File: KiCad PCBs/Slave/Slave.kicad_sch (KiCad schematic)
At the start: 47 parts, among them J1 Screw_Terminal_01x02, J10 AVR-ISP-6, J11 Conn_01x06_Female, J12 Screw_Terminal_01x02, J13 Screw_Terminal_01x02, J14 Screw_Terminal_01x02, J15 Screw_Terminal_01x02, J16 Screw_Terminal_01x02, J2 Screw_Terminal_01x02, J3 Screw_Terminal_01x02, J4 Screw_Terminal_01x02, J5 Screw_Terminal_01x02, J6 Screw_Terminal_01x02, J7 Screw_Terminal_01x02, J8 Screw_Terminal_01x02, J9 Screw_Terminal_01x02, SW1 SW_DIP_x02, SW2 SW_DIP_x02, SW3 SW_MEC_5E, U1 ATmega328P-AU, U2 MAX487ESA+T, U3 ULN2003A, U5 AMS1117-5.0, Y1 Crystal_GND24

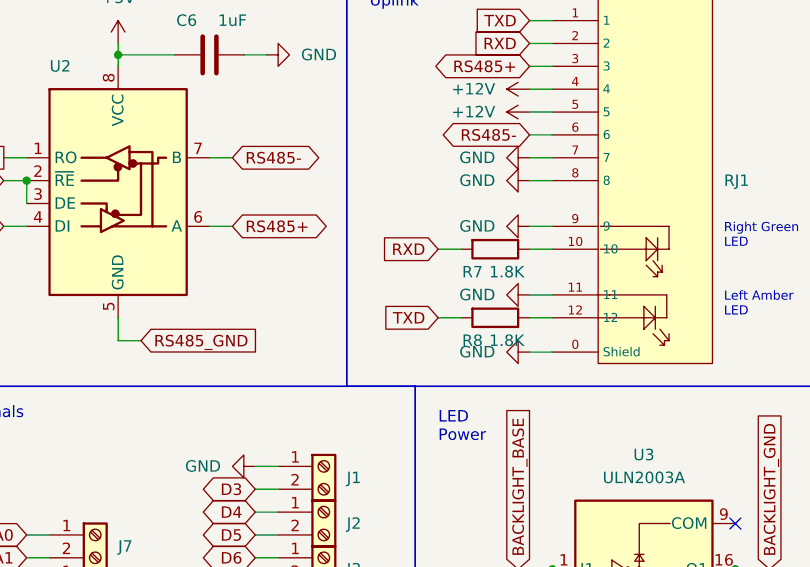
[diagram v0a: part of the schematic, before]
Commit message: Fixed swapped LEDs on Slave
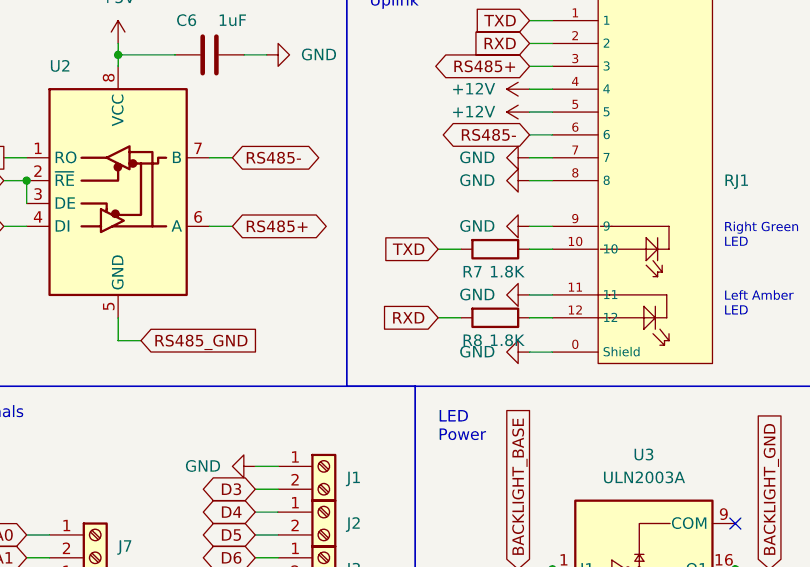
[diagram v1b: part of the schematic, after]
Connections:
- net RXD: now also R8.2; no longer R7.2
- net TXD: now also R7.2; no longer R8.2
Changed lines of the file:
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@@
+    )
+  )
+  (global_label "TXD" (shape input) (at 242.57 43.18 180) (fields_autoplaced)
+    (effects (font (size 1.27 1.27)) (justify right))
+    (property "Intersheet References" "${INTERSHEET_REFS}" (id 0) (at 236.7098 43.1006 0)
+      (effects (font (size 1.27 1.27)) (justify right) hide)
     )
   )
@@
     )
   )
-  (global_label "TXD" (shape input) (at 242.57 50.8 180) (fields_autoplaced)
-    (effects (font (size 1.27 1.27)) (justify right))
-    (property "Intersheet References" "${INTERSHEET_REFS}" (id 0) (at 236.7098 50.7206 0)
-      (effects (font (size 1.27 1.27)) (justify right) hide)
-    )
-  )
   (global_label "D10" (shape bidirectional) (at 222.25 87.63 180) (fields_autoplaced)
     (effects (font (size 1.27 1.27)) (justify right))
@@
     )
   )
-  (global_label "RXD" (shape input) (at 242.57 43.18 180) (fields_autoplaced)
-    (effects (font (size 1.27 1.27)) (justify right))
-    (property "Intersheet References" "${INTERSHEET_REFS}" (id 0) (at 236.4074 43.1006 0)
-      (effects (font (size 1.27 1.27)) (justify right) hide)
-    )
-  )
   (global_label "A3" (shape bidirectional) (at 196.85 82.55 180) (fields_autoplaced)
     (effects (font (size 1.27 1.27)) (justify right))
@@
       (effects (font (size 1.27 1.27)) (justify right) hide)
     )
+  )
+  (global_label "RXD" (shape input) (at 242.57 50.8 180) (fields_autoplaced)
+    (effects (font (size 1.27 1.27)) (justify right))
+    (property "Intersheet References" "${INTERSHEET_REFS}" (id 0) (at 236.4074 50.7206 0)
+      (effects (font (size 1.27 1.27)) (justify right) hide)
+    )

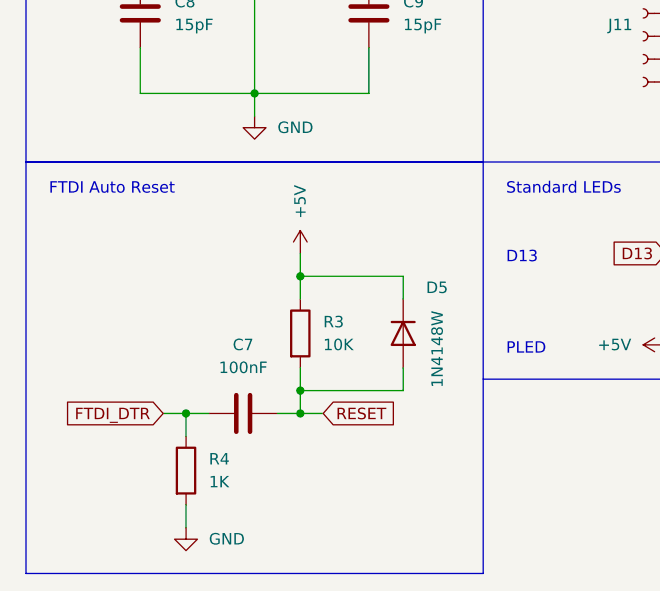
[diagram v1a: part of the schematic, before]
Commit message: Removed unnecessary resistor
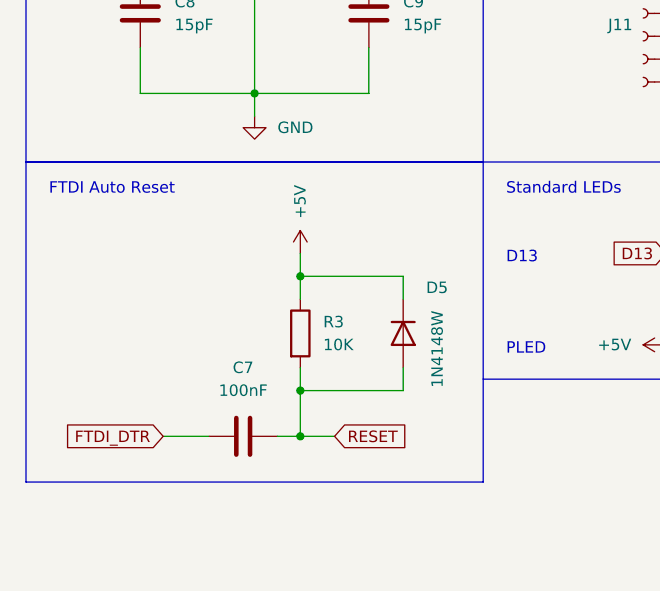
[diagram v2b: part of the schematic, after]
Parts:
- removed R4: 1K, Resistor_SMD:R_0805_2012Metric, symbol Device:R
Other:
- moved on the sheet: C7
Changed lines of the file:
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@@
   (junction (at 38.1 78.74) (diameter 0) (color 0 0 0 0)
   )
-  (junction (at 43.18 154.94) (diameter 0) (color 0 0 0 0)
+  (junction (at 43.18 157.48) (diameter 0) (color 0 0 0 0)
   )
   (junction (at 87.63 35.56) (diameter 0) (color 0 0 0 0)
@@
   (junction (at 27.94 35.56) (diameter 0) (color 0 0 0 0)
   )
-  (junction (at 30.48 154.94) (diameter 0) (color 0 0 0 0)
-  )
   (no_connect (at 48.26 22.86))
   (no_connect (at 133.35 69.85))
@@
     (stroke (width 0) (type default) (color 0 0 0 0))
   )
-  (wire (pts (xy 43.18 154.94) (xy 43.18 152.4))
+  (wire (pts (xy 43.18 157.48) (xy 43.18 152.4))
     (stroke (width 0) (type default) (color 0 0 0 0))
   )
@@
     (stroke (width 0) (type default) (color 0 0 0 0))
   )
-  (wire (pts (xy 30.48 154.94) (xy 33.02 154.94))
-    (stroke (width 0) (type default) (color 0 0 0 0))
-  )
   (polyline (pts (xy 185.42 12.7) (xy 185.42 41.91))
     (stroke (width 0) (type default) (color 0 0 0 0))
@@
     (stroke (width 0) (type default) (color 0 0 0 0))
   )
-  (wire (pts (xy 27.94 154.94) (xy 30.48 154.94))
+  (wire (pts (xy 27.94 157.48) (xy 33.02 157.48))
     (stroke (width 0) (type default) (color 0 0 0 0))
   )
@@
     (stroke (width 0) (type default) (color 0 0 0 0))
   )
-  (polyline (pts (xy 12.7 127) (xy 12.7 172.72))
+  (polyline (pts (xy 12.7 127) (xy 12.7 162.56))
     (stroke (width 0) (type default) (color 0 0 0 0))
   )
@@
     (stroke (width 0) (type default) (color 0 0 0 0))
   )
-  (polyline (pts (xy 63.5 172.72) (xy 12.7 172.72))
+  (polyline (pts (xy 63.5 162.56) (xy 12.7 162.56))
     (stroke (width 0) (type default) (color 0 0 0 0))
   )
@@
     (stroke (width 0) (type default) (color 0 0 0 0))
   )
-  (wire (pts (xy 30.48 167.64) (xy 30.48 165.1))
-    (stroke (width 0) (type default) (color 0 0 0 0))
-  )
   (wire (pts (xy 50.8 101.6) (xy 53.34 101.6))
     (stroke (width 0) (type default) (color 0 0 0 0))
@@
     (stroke (width 0) (type default) (color 0 0 0 0))
   )
-  (wire (pts (xy 30.48 154.94) (xy 30.48 157.48))
-    (stroke (width 0) (type default) (color 0 0 0 0))
-  )
   (wire (pts (xy 224.79 111.76) (xy 224.79 114.3))
     (stroke (width 0) (type default) (color 0 0 0 0))
@@
     (stroke (width 0) (type default) (color 0 0 0 0))
   )
-  (polyline (pts (xy 63.5 127) (xy 63.5 172.72))
+  (polyline (pts (xy 63.5 127) (xy 63.5 162.56))
     (stroke (width 0) (type default) (color 0 0 0 0))
   )
@@
     (stroke (width 0) (type default) (color 0 0 0 0))
   )
-  (wire (pts (xy 43.18 154.94) (xy 45.72 154.94))
+  (wire (pts (xy 43.18 157.48) (xy 46.99 157.48))
     (stroke (width 0) (type default) (color 0 0 0 0))
   )
@@
     (stroke (width 0) (type default) (color 0 0 0 0))
   )
-  (wire (pts (xy 40.64 154.94) (xy 43.18 154.94))
+  (wire (pts (xy 40.64 157.48) (xy 43.18 157.48))
     (stroke (width 0) (type default) (color 0 0 0 0))
   )
@@
     )
   )
-  (global_label "FTDI_DTR" (shape input) (at 27.94 154.94 180) (fields_autoplaced)
+  (global_label "FTDI_DTR" (shape input) (at 27.94 157.48 180) (fields_autoplaced)
     (effects (font (size 1.27 1.27)) (justify right))
-    (property "Intersheet References" "${INTERSHEET_REFS}" (id 0) (at 17.1207 154.8606 0)
+    (property "Intersheet References" "${INTERSHEET_REFS}" (id 0) (at 17.1207 157.4006 0)
       (effects (font (size 1.27 1.27)) (justify right) hide)
     )
@@
     )
   )
-  (global_label "RESET" (shape input) (at 45.72 154.94 0) (fields_autoplaced)
+  (global_label "RESET" (shape input) (at 46.99 157.48 0) (fields_autoplaced)
     (effects (font (size 1.27 1.27)) (justify left))
-    (property "Intersheet References" "${INTERSHEET_REFS}" (id 0) (at 53.8783 154.8606 0)
+    (property "Intersheet References" "${INTERSHEET_REFS}" (id 0) (at 55.1483 157.4006 0)
       (effects (font (size 1.27 1.27)) (justify left) hide)
     )
@@
     (pin "4")
   )
-  (symbol (lib_id "Device:C") (at 36.83 154.94 270) (unit 1)
+  (symbol (lib_id "Device:C") (at 36.83 157.48 270) (unit 1)
     (in_bom yes) (on_board yes) (fields_autoplaced)
-    (property "Reference" "C7" (id 0) (at 36.83 147.32 90))
-    (property "Value" "100nF" (id 1) (at 36.83 149.86 90))
-    (property "Footprint" "A10 KiCad Libraries:C0402" (id 2) (at 33.02 155.9052 0)
+    (property "Reference" "C7" (id 0) (at 36.83 149.86 90))
+    (property "Value" "100nF" (id 1) (at 36.83 152.4 90))
+    (property "Footprint" "A10 KiCad Libraries:C0402" (id 2) (at 33.02 158.4452 0)
       (effects (font (size 1.27 1.27)) hide)
     )
-    (property "Datasheet" "~" (id 3) (at 36.83 154.94 0)
+    (property "Datasheet" "~" (id 3) (at 36.83 157.48 0)
       (effects (font (size 1.27 1.27)) hide)
     )
-    (property "LCSC" "C1525" (id 4) (at 36.83 154.94 0)
+    (property "LCSC" "C1525" (id 4) (at 36.83 157.48 0)
       (effects (font (size 1.27 1.27)) hide)
     )
@@
     (pin "2")
   )
-  (symbol (lib_id "Device:R") (at 30.48 161.29 0) (unit 1)
-    (in_bom yes) (on_board yes) (fields_autoplaced)
-    (property "Reference" "R4" (id 0) (at 33.02 160.0199 0)
-      (effects (font (size 1.27 1.27)) (justify left))
-    )
-    (property "Value" "1K" (id 1) (at 33.02 162.5599 0)
-      (effects (font (size 1.27 1.27)) (justify left))
-    )
-    (property "Footprint" "Resistor_SMD:R_0805_2012Metric" (id 2) (at 28.702 161.29 90)
-      (effects (font (size 1.27 1.27)) hide)
-    )
-    (property "Datasheet" "~" (id 3) (at 30.48 161.29 0)
-      (effects (font (size 1.27 1.27)) hide)
-    )
-    (property "LCSC" "C17513" (id 4) (at 30.48 161.29 0)
-      (effects (font (size 1.27 1.27)) hide)
-    )
-    (pin "1")
-    (pin "2")
-  )
   (symbol (lib_id "Connector:Screw_Terminal_01x02") (at 201.93 119.38 270) (unit 1)
     (in_bom yes) (on_board yes)
@@
     (pin "3")
   )
-  (symbol (lib_id "power:GND") (at 30.48 167.64 0) (unit 1)
-    (in_bom yes) (on_board yes) (fields_autoplaced)
-    (property "Reference" "#PWR0102" (id 0) (at 30.48 173.99 0)
-      (effects (font (size 1.27 1.27)) hide)
-    )
-    (property "Value" "GND" (id 1) (at 33.02 168.9099 0)
-      (effects (font (size 1.27 1.27)) (justify left))
-    )
-    (property "Footprint" "" (id 2) (at 30.48 167.64 0)
-      (effects (font (size 1.27 1.27)) hide)
-    )
-    (property "Datasheet" "" (id 3) (at 30.48 167.64 0)
-      (effects (font (size 1.27 1.27)) hide)
-    )
-    (pin "1")
-  )
   (symbol (lib_id "Device:C_Polarized") (at 68.58 31.75 0) (unit 1)
     (in_bom yes) (on_board yes)
@@
       (reference "#PWR0101") (unit 1) (value "+5V") (footprint "")
     )
-    (path "/df391fcf-55bf-4a0a-9ae3-03317be1cd1b"
-      (reference "#PWR0102") (unit 1) (value "GND") (footprint "")
-    )
     (path "/1d7d13da-6155-4f5e-b055-b0667fd2dc2b"
       (reference "#PWR0103") (unit 1) (value "+12V") (footprint "")
@@
       (reference "R3") (unit 1) (value "10K") (footprint "Resistor_SMD:R_0805_2012Metric")
     )
-    (path "/8bcfb1df-912c-426b-8aa1-f6f018b56734"
-      (reference "R4") (unit 1) (value "1K") (footprint "Resistor_SMD:R_0805_2012Metric")
-    )
     (path "/74626994-d95b-4d1a-80b6-3bebb0f869ed"

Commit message: Include headers in BOM
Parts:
- J10, J11: now in the parts list
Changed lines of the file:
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@@
   )
   (symbol (lib_id "Connector:AVR-ISP-6") (at 87.63 74.93 0) (unit 1)
-    (in_bom no) (on_board yes) (fields_autoplaced)
+    (in_bom yes) (on_board yes) (fields_autoplaced)
     (property "Reference" "J10" (id 0) (at 78.74 72.3899 0)
       (effects (font (size 1.27 1.27)) (justify right))
@@
   )
   (symbol (lib_id "Connector:Conn_01x06_Female") (at 81.28 110.49 0) (mirror y) (unit 1)
-    (in_bom no) (on_board yes)
+    (in_bom yes) (on_board yes)
     (property "Reference" "J11" (id 0) (at 78.74 111.76 0))
     (property "Value" "Conn_01x06_Female" (id 1) (at 80.01 113.0299 0)

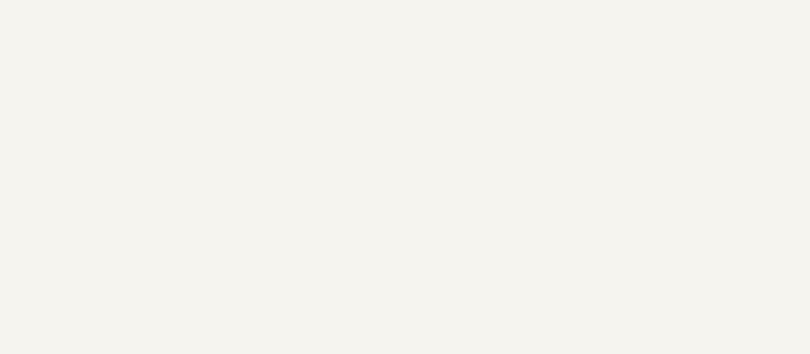
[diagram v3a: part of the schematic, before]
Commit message: Added Mounting Holes to Slave PCB Added External Connection PCB
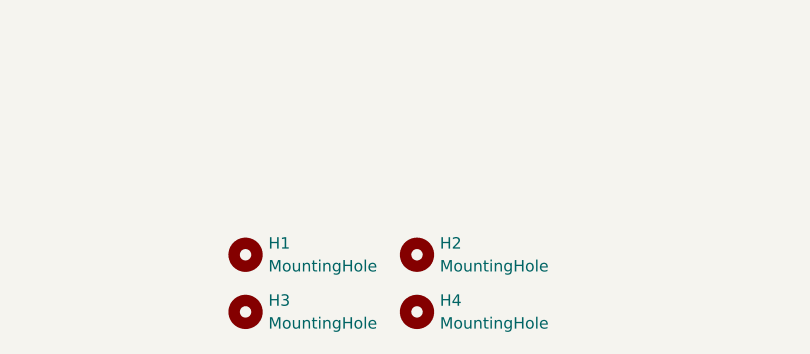
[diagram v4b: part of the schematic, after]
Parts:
- added H1, H2, H3, H4: MountingHole, MountingHole:MountingHole_3.2mm_M3, symbol Mechanical:MountingHole
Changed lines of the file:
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@@
     (pin "2")
+  )
+  (symbol (lib_id "Mechanical:MountingHole") (at 157.48 191.77 0) (unit 1)
+    (in_bom yes) (on_board yes) (fields_autoplaced)
+    (property "Reference" "H4" (id 0) (at 160.02 190.4999 0)
+      (effects (font (size 1.27 1.27)) (justify left))
+    )
+    (property "Value" "MountingHole" (id 1) (at 160.02 193.0399 0)
+      (effects (font (size 1.27 1.27)) (justify left))
+    )
+    (property "Footprint" "MountingHole:MountingHole_3.2mm_M3" (id 2) (at 157.48 191.77 0)
+      (effects (font (size 1.27 1.27)) hide)
+    )
+    (property "Datasheet" "~" (id 3) (at 157.48 191.77 0)
+      (effects (font (size 1.27 1.27)) hide)
+    )
   )
   (symbol (lib_id "Device:C") (at 52.07 69.85 0) (unit 1)
@@
     (pin "2")
   )
+  (symbol (lib_id "Mechanical:MountingHole") (at 138.43 191.77 0) (unit 1)
+    (in_bom yes) (on_board yes) (fields_autoplaced)
+    (property "Reference" "H3" (id 0) (at 140.97 190.4999 0)
+      (effects (font (size 1.27 1.27)) (justify left))
+    )
+    (property "Value" "MountingHole" (id 1) (at 140.97 193.0399 0)
+      (effects (font (size 1.27 1.27)) (justify left))
+    )
+    (property "Footprint" "MountingHole:MountingHole_3.2mm_M3" (id 2) (at 138.43 191.77 0)
+      (effects (font (size 1.27 1.27)) hide)
+    )
+    (property "Datasheet" "~" (id 3) (at 138.43 191.77 0)
+      (effects (font (size 1.27 1.27)) hide)
+    )
+  )
   (symbol (lib_id "Device:C") (at 25.4 110.49 180) (unit 1)
     (in_bom yes) (on_board yes) (fields_autoplaced)
@@
     (pin "1")
     (pin "2")
+  )
+  (symbol (lib_id "Mechanical:MountingHole") (at 157.48 185.42 0) (unit 1)
+    (in_bom yes) (on_board yes) (fields_autoplaced)
+    (property "Reference" "H2" (id 0) (at 160.02 184.1499 0)
+      (effects (font (size 1.27 1.27)) (justify left))
+    )
+    (property "Value" "MountingHole" (id 1) (at 160.02 186.6899 0)
+      (effects (font (size 1.27 1.27)) (justify left))
+    )
+    (property "Footprint" "MountingHole:MountingHole_3.2mm_M3" (id 2) (at 157.48 185.42 0)
+      (effects (font (size 1.27 1.27)) hide)
+    )
+    (property "Datasheet" "~" (id 3) (at 157.48 185.42 0)
+      (effects (font (size 1.27 1.27)) hide)
+    )
   )
   (symbol (lib_id "Device:R") (at 158.75 24.13 270) (unit 1)
@@
     (pin "3")
   )
+  (symbol (lib_id "Mechanical:MountingHole") (at 138.43 185.42 0) (unit 1)
+    (in_bom yes) (on_board yes) (fields_autoplaced)
+    (property "Reference" "H1" (id 0) (at 140.97 184.1499 0)
+      (effects (font (size 1.27 1.27)) (justify left))
+    )
+    (property "Value" "MountingHole" (id 1) (at 140.97 186.6899 0)
+      (effects (font (size 1.27 1.27)) (justify left))
+    )
+    (property "Footprint" "MountingHole:MountingHole_3.2mm_M3" (id 2) (at 138.43 185.42 0)
+      (effects (font (size 1.27 1.27)) hide)
+    )
+    (property "Datasheet" "~" (id 3) (at 138.43 185.42 0)
+      (effects (font (size 1.27 1.27)) hide)
+    )
+  )
   (symbol (lib_id "Device:C_Polarized") (at 68.58 31.75 0) (unit 1)
     (in_bom yes) (on_board yes)
@@
       (reference "D5") (unit 1) (value "1N4148W") (footprint "Diode_SMD:D_SOD-123")
     )
+    (path "/df46ce7b-e294-4eb5-aad3-c06adf119d17"
+      (reference "H1") (unit 1) (value "MountingHole") (footprint "MountingHole:MountingHole_3.2mm_M3")
+    )
+    (path "/788048e6-a1ad-4091-ba5b-82fb121bfcd4"
+      (reference "H2") (unit 1) (value "MountingHole") (footprint "MountingHole:MountingHole_3.2mm_M3")
+    )
+    (path "/6da90eb4-a554-4792-af50-87b94d882684"
+      (reference "H3") (unit 1) (value "MountingHole") (footprint "MountingHole:MountingHole_3.2mm_M3")
+    )
+    (path "/2e38d38b-9e78-482f-9dfb-40748af35568"
+      (reference "H4") (unit 1) (value "MountingHole") (footprint "MountingHole:MountingHole_3.2mm_M3")
+    )
     (path "/bcbcd1cd-faf4-44e1-af84-464c8f6f2585"
